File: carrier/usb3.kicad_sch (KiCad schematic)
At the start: 48 parts, among them J13 USB3_A, U16 W25X40CLUXIG, U18 AP2191, U19 uPD720202, U5 TPD4EUSB30, Y1 24MHz

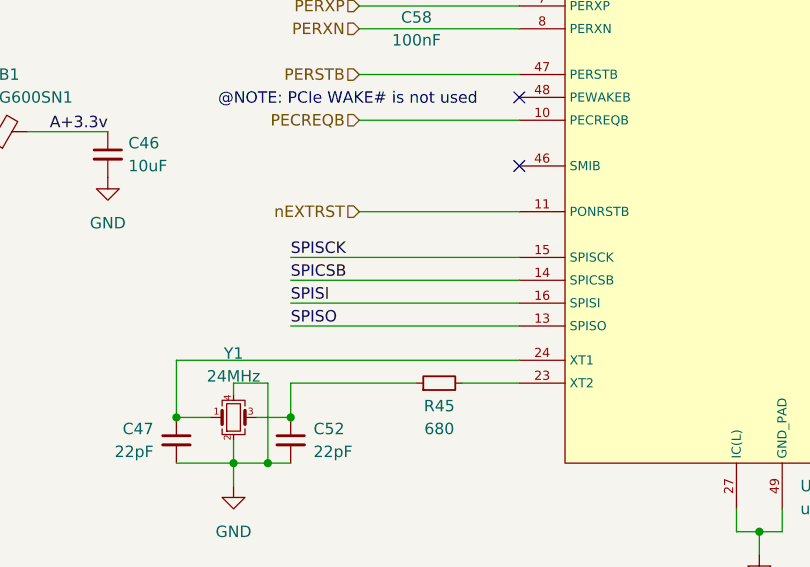
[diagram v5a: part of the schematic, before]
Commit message: Feat[carrier]: v3 ordered
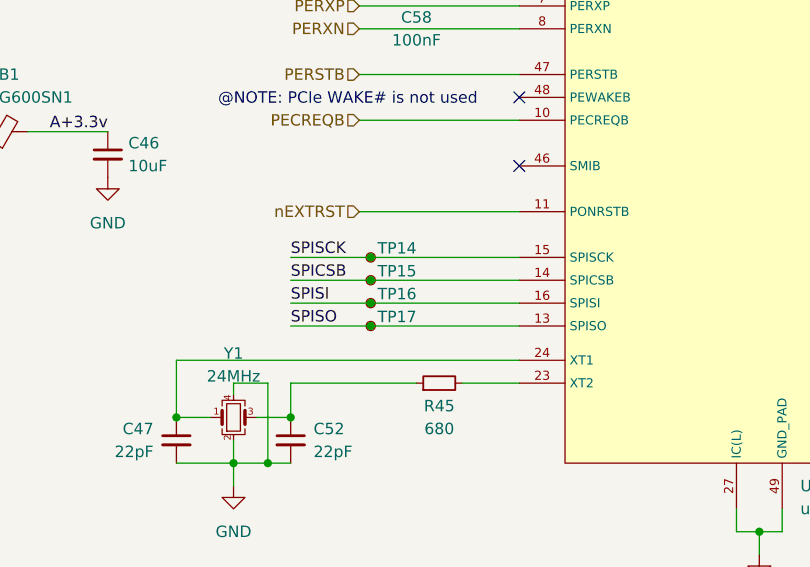
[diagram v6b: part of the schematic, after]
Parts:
- added TP14, TP15, TP16, TP17: ~, TestPoint:TestPoint_Pad_D1.5mm, symbol Connector:TestPoint_Small
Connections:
- net SPICSB: now also TP15.1
- net SPISCK: now also TP14.1
- net SPISI: now also TP16.1
- net SPISO: now also TP17.1
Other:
- company: (none) -> MUREX Robotics [Byran Huang]
- title: (none) -> Carrier Board
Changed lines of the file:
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@@
 (kicad_sch (version 20230819) (generator eeschema)
   (paper "A4")
+  (title_block
+    (title "Carrier Board")
+    (date "2023-12-09")
+    (rev "V3")
+    (company "MUREX Robotics [Byran Huang]")
+    (comment 1 "//DO IT RIGHT,  DO IT MUREX")
+    (comment 2 "// ATTEMPT THE IMPOSSIBLE")
+    (comment 3 "CM4-based ROV (robotics) control board.")
+    (comment 4 "The MUREX Carrier Board is the world's first open-source ")
+  )
   (junction (at 45.72 26.67) (diameter 0) (color 0 0 0 0)
   )
@@
   (junction (at 45.72 41.91) (diameter 0) (color 0 0 0 0)
   )
+  (junction (at 85.09 92.71) (diameter 0) (color 0 0 0 0)
+  )
   (junction (at 204.47 86.36) (diameter 0) (color 0 0 0 0)
   )
@@
   (junction (at 128.27 123.19) (diameter 0) (color 0 0 0 0)
   )
+  (junction (at 85.09 100.33) (diameter 0) (color 0 0 0 0)
+  )
   (junction (at 106.68 31.75) (diameter 0) (color 0 0 0 0)
   )
@@
   (junction (at 63.5 110.49) (diameter 0) (color 0 0 0 0)
   )
+  (junction (at 85.09 97.79) (diameter 0) (color 0 0 0 0)
+  )
   (junction (at 35.56 26.67) (diameter 0) (color 0 0 0 0)
   )
@@
   )
   (junction (at 86.36 26.67) (diameter 0) (color 0 0 0 0)
+  )
+  (junction (at 85.09 95.25) (diameter 0) (color 0 0 0 0)
   )
   (junction (at 156.21 31.75) (diameter 0) (color 0 0 0 0)
@@
     (stroke (width 0) (type default))
   )
+  (wire (pts (xy 85.09 97.79) (xy 101.6 97.79))
+    (stroke (width 0) (type default))
+  )
   (wire (pts (xy 86.36 41.91) (xy 96.52 41.91))
     (stroke (width 0) (type default))
@@
     (stroke (width 0) (type default))
   )
-  (wire (pts (xy 76.2 92.71) (xy 101.6 92.71))
+  (wire (pts (xy 76.2 92.71) (xy 85.09 92.71))
     (stroke (width 0) (type default))
   )
@@
     (stroke (width 0) (type default))
   )
-  (wire (pts (xy 76.2 95.25) (xy 101.6 95.25))
+  (wire (pts (xy 76.2 95.25) (xy 85.09 95.25))
     (stroke (width 0) (type default))
   )
@@
     (stroke (width 0) (type default))
   )
+  (wire (pts (xy 85.09 95.25) (xy 101.6 95.25))
+    (stroke (width 0) (type default))
+  )
   (wire (pts (xy 63.5 115.57) (xy 69.85 115.57))
     (stroke (width 0) (type default))
@@
     (stroke (width 0) (type default))
   )
-  (wire (pts (xy 76.2 97.79) (xy 101.6 97.79))
+  (wire (pts (xy 85.09 92.71) (xy 101.6 92.71))
+    (stroke (width 0) (type default))
+  )
+  (wire (pts (xy 76.2 97.79) (xy 85.09 97.79))
     (stroke (width 0) (type default))
   )
@@
     (stroke (width 0) (type default))
   )
+  (wire (pts (xy 85.09 100.33) (xy 101.6 100.33))
+    (stroke (width 0) (type default))
+  )
   (wire (pts (xy 154.94 76.2) (xy 166.37 76.2))
     (stroke (width 0) (type default))
@@
     (stroke (width 0) (type default))
   )
-  (wire (pts (xy 76.2 100.33) (xy 101.6 100.33))
+  (wire (pts (xy 76.2 100.33) (xy 85.09 100.33))
     (stroke (width 0) (type default))
   )
@@
         (path "/4b1cea9d-93bc-4380-88c3-ede99bb53de2/4da56470-0b67-4551-923f-8b4b216ded57/7428a731-2323-481a-bc64-c9fb631cc98e"
           (reference "R50") (unit 1)
+        )
+      )
+    )
+  )
+  (symbol (lib_id "Connector:TestPoint_Small") (at 85.09 100.33 180) (unit 1)
+    (exclude_from_sim no) (in_bom yes) (on_board yes) (dnp no)
+    (property "Reference" "TP17" (at 85.852 99.314 0)
+      (effects (font (size 1.27 1.27)) (justify right))
+    )
+    (property "Value" "~" (at 83.82 99.0601 0)
+      (effects (font (size 1.27 1.27)) (justify left))
+    )
+    (property "Footprint" "TestPoint:TestPoint_Pad_D1.5mm" (at 80.01 100.33 0)
+      (effects (font (size 1.27 1.27)) hide)
+    )
+    (property "Datasheet" "~" (at 80.01 100.33 0)
+      (effects (font (size 1.27 1.27)) hide)
+    )
+    (property "Description" "test point" (at 85.09 100.33 0)
+      (effects (font (size 1.27 1.27)) hide)
+    )
+    (pin "1")
+    (instances
+      (project "carrier"
+        (path "/4b1cea9d-93bc-4380-88c3-ede99bb53de2/4da56470-0b67-4551-923f-8b4b216ded57/7428a731-2323-481a-bc64-c9fb631cc98e"
+          (reference "TP17") (unit 1)
+        )
+      )
+    )
+  )
+  (symbol (lib_id "Connector:TestPoint_Small") (at 85.09 92.71 180) (unit 1)
+    (exclude_from_sim no) (in_bom yes) (on_board yes) (dnp no)
+    (property "Reference" "TP14" (at 85.852 91.694 0)
+      (effects (font (size 1.27 1.27)) (justify right))
+    )
+    (property "Value" "~" (at 83.82 91.4401 0)
+      (effects (font (size 1.27 1.27)) (justify left))
+    )
+    (property "Footprint" "TestPoint:TestPoint_Pad_D1.5mm" (at 80.01 92.71 0)
+      (effects (font (size 1.27 1.27)) hide)
+    )
+    (property "Datasheet" "~" (at 80.01 92.71 0)
+      (effects (font (size 1.27 1.27)) hide)
+    )
+    (property "Description" "test point" (at 85.09 92.71 0)
+      (effects (font (size 1.27 1.27)) hide)
+    )
+    (pin "1")
+    (instances
+      (project "carrier"
+        (path "/4b1cea9d-93bc-4380-88c3-ede99bb53de2/4da56470-0b67-4551-923f-8b4b216ded57/7428a731-2323-481a-bc64-c9fb631cc98e"
+          (reference "TP14") (unit 1)
         )
       )
@@
     )
   )
+  (symbol (lib_id "Connector:TestPoint_Small") (at 85.09 97.79 180) (unit 1)
+    (exclude_from_sim no) (in_bom yes) (on_board yes) (dnp no)
+    (property "Reference" "TP16" (at 85.852 96.774 0)
+      (effects (font (size 1.27 1.27)) (justify right))
+    )
+    (property "Value" "~" (at 83.82 96.5201 0)
+      (effects (font (size 1.27 1.27)) (justify left))
+    )
+    (property "Footprint" "TestPoint:TestPoint_Pad_D1.5mm" (at 80.01 97.79 0)
+      (effects (font (size 1.27 1.27)) hide)
+    )
+    (property "Datasheet" "~" (at 80.01 97.79 0)
+      (effects (font (size 1.27 1.27)) hide)
+    )
+    (property "Description" "test point" (at 85.09 97.79 0)
+      (effects (font (size 1.27 1.27)) hide)
+    )
+    (pin "1")
+    (instances
+      (project "carrier"
+        (path "/4b1cea9d-93bc-4380-88c3-ede99bb53de2/4da56470-0b67-4551-923f-8b4b216ded57/7428a731-2323-481a-bc64-c9fb631cc98e"
+          (reference "TP16") (unit 1)
+        )
+      )
+    )
+  )
   (symbol (lib_id "power:GND") (at 69.85 118.11 0) (unit 1)
     (exclude_from_sim no) (in_bom yes) (on_board yes) (dnp no) (fields_autoplaced)
@@
         )
       )
+    )
+  )
+  (symbol (lib_id "Connector:TestPoint_Small") (at 85.09 95.25 180) (unit 1)
+    (exclude_from_sim no) (in_bom yes) (on_board yes) (dnp no)
+    (property "Reference" "TP15" (at 85.852 94.234 0)
+      (effects (font (size 1.27 1.27)) (justify right))
+    )
+    (property "Value" "~" (at 83.82 93.9801 0)
+      (effects (font (size 1.27 1.27)) (justify left))
+    )
+    (property "Footprint" "TestPoint:TestPoint_Pad_D1.5mm" (at 80.01 95.25 0)
+      (effects (font (size 1.27 1.27)) hide)
+    )
+    (property "Datasheet" "~" (at 80.01 95.25 0)
+      (effects (font (size 1.27 1.27)) hide)
+    )
+    (property "Description" "test point" (at 85.09 95.25 0)
+      (effects (font (size 1.27 1.27)) hide)
+    )
+    (pin "1")
+    (instances
+      (project "carrier"
+        (path "/4b1cea9d-93bc-4380-88c3-ede99bb53de2/4da56470-0b67-4551-923f-8b4b216ded57/7428a731-2323-481a-bc64-c9fb631cc98e"
+          (reference "TP15") (unit 1)
+        )
+      )

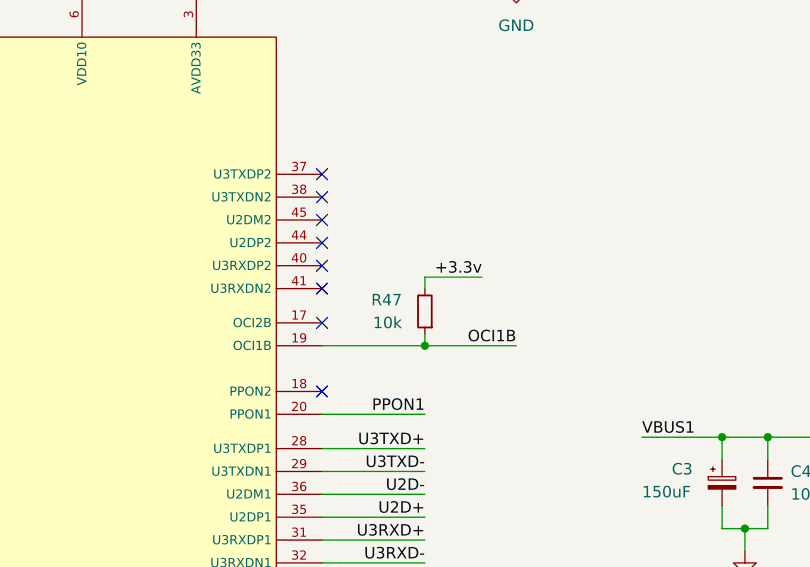
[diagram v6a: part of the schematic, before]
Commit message: Fix: updated carrier board to v3.1
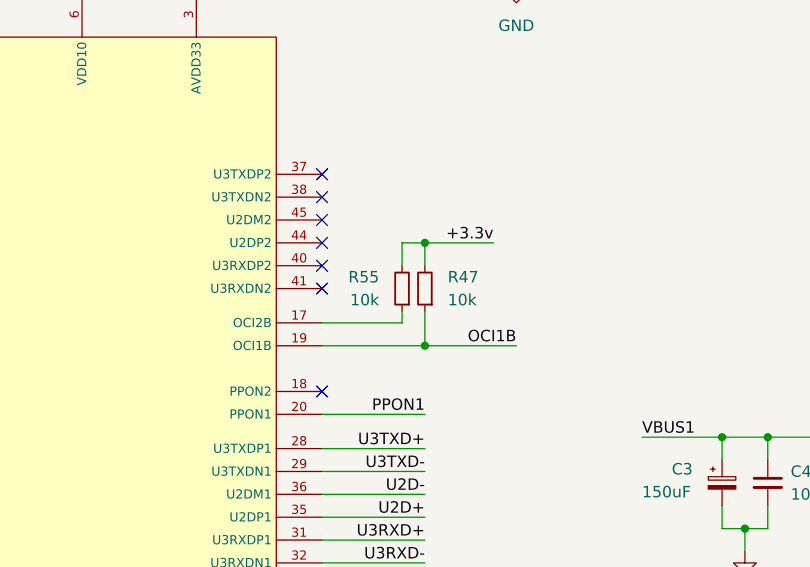
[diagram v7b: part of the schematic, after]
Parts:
- added R55: 10k, Resistor_SMD:R_0402_1005Metric, symbol Device:R_Small
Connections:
- net +3.3v: now also R55.2
- net at U19.17 (OCI2B): now also R55.1
- no-connect marks 12 -> 11
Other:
- moved on the sheet: R47
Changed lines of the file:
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@@
   (title_block
     (title "Carrier Board")
-    (date "2023-12-09")
-    (rev "V3")
+    (date "2023-12-30")
+    (rev "V3.1")
     (company "MUREX Robotics [Byran Huang]")
     (comment 1 "//DO IT RIGHT,  DO IT MUREX")
@@
   (junction (at 96.52 26.67) (diameter 0) (color 0 0 0 0)
   )
+  (junction (at 166.37 64.77) (diameter 0) (color 0 0 0 0)
+  )
   (junction (at 201.93 96.52) (diameter 0) (color 0 0 0 0)
   )
@@
   (no_connect (at 154.94 57.15))
   (no_connect (at 154.94 64.77))
-  (no_connect (at 154.94 73.66))
   (no_connect (at 101.6 82.55))
   (no_connect (at 101.6 74.93))
@@
     (stroke (width 0) (type default))
   )
-  (wire (pts (xy 166.37 74.93) (xy 166.37 76.2))
+  (wire (pts (xy 166.37 72.39) (xy 166.37 76.2))
     (stroke (width 0) (type default))
   )
@@
     (stroke (width 0) (type default))
   )
+  (wire (pts (xy 154.94 73.66) (xy 163.83 73.66))
+    (stroke (width 0) (type default))
+  )
   (wire (pts (xy 72.39 110.49) (xy 76.2 110.49))
     (stroke (width 0) (type default))
@@
     (stroke (width 0) (type default))
   )
-  (wire (pts (xy 166.37 68.58) (xy 172.72 68.58))
+  (wire (pts (xy 166.37 64.77) (xy 173.99 64.77))
     (stroke (width 0) (type default))
   )
@@
     (stroke (width 0) (type default))
   )
+  (wire (pts (xy 163.83 72.39) (xy 163.83 73.66))
+    (stroke (width 0) (type default))
+  )
   (wire (pts (xy 190.5 86.36) (xy 199.39 86.36))
     (stroke (width 0) (type default))
@@
     (stroke (width 0) (type default))
   )
+  (wire (pts (xy 163.83 67.31) (xy 163.83 64.77))
+    (stroke (width 0) (type default))
+  )
   (wire (pts (xy 176.53 31.75) (xy 176.53 35.56))
     (stroke (width 0) (type default))
@@
     (stroke (width 0) (type default))
   )
-  (wire (pts (xy 166.37 68.58) (xy 166.37 69.85))
+  (wire (pts (xy 166.37 64.77) (xy 166.37 67.31))
+    (stroke (width 0) (type default))
+  )
+  (wire (pts (xy 163.83 64.77) (xy 166.37 64.77))
     (stroke (width 0) (type default))
   )
@@
     (effects (font (size 1.27 1.27)) (justify left bottom))
   )
-  (label "+3.3v" (at 172.72 68.58 180) (fields_autoplaced)
+  (label "+3.3v" (at 173.99 64.77 180) (fields_autoplaced)
     (effects (font (size 1.27 1.27)) (justify right bottom))
   )
@@
     )
   )
-  (symbol (lib_id "Device:R_Small") (at 166.37 72.39 180) (unit 1)
-    (exclude_from_sim no) (in_bom yes) (on_board yes) (dnp no) (fields_autoplaced)
-    (property "Reference" "R47" (at 163.83 71.1199 0)
-      (effects (font (size 1.27 1.27)) (justify left))
-    )
-    (property "Value" "10k" (at 163.83 73.6599 0)
-      (effects (font (size 1.27 1.27)) (justify left))
-    )
-    (property "Footprint" "Resistor_SMD:R_0402_1005Metric" (at 166.37 72.39 0)
-      (effects (font (size 1.27 1.27)) hide)
-    )
-    (property "Datasheet" "~" (at 166.37 72.39 0)
-      (effects (font (size 1.27 1.27)) hide)
-    )
-    (property "Description" "Resistor, small symbol" (at 166.37 72.39 0)
+  (symbol (lib_id "Device:R_Small") (at 166.37 69.85 180) (unit 1)
+    (exclude_from_sim no) (in_bom yes) (on_board yes) (dnp no) (fields_autoplaced)
+    (property "Reference" "R47" (at 168.91 68.5799 0)
+      (effects (font (size 1.27 1.27)) (justify right))
+    )
+    (property "Value" "10k" (at 168.91 71.1199 0)
+      (effects (font (size 1.27 1.27)) (justify right))
+    )
+    (property "Footprint" "Resistor_SMD:R_0402_1005Metric" (at 166.37 69.85 0)
+      (effects (font (size 1.27 1.27)) hide)
+    )
+    (property "Datasheet" "~" (at 166.37 69.85 0)
+      (effects (font (size 1.27 1.27)) hide)
+    )
+    (property "Description" "Resistor, small symbol" (at 166.37 69.85 0)
       (effects (font (size 1.27 1.27)) hide)
     )
@@
         )
       )
+    )
+  )
+  (symbol (lib_id "Device:R_Small") (at 163.83 69.85 180) (unit 1)
+    (exclude_from_sim no) (in_bom yes) (on_board yes) (dnp no) (fields_autoplaced)
+    (property "Reference" "R55" (at 161.29 68.5799 0)
+      (effects (font (size 1.27 1.27)) (justify left))
+    )
+    (property "Value" "10k" (at 161.29 71.1199 0)
+      (effects (font (size 1.27 1.27)) (justify left))
+    )
+    (property "Footprint" "Resistor_SMD:R_0402_1005Metric" (at 163.83 69.85 0)
+      (effects (font (size 1.27 1.27)) hide)
+    )
+    (property "Datasheet" "~" (at 163.83 69.85 0)
+      (effects (font (size 1.27 1.27)) hide)
+    )
+    (property "Description" "Resistor, small symbol" (at 163.83 69.85 0)
+      (effects (font (size 1.27 1.27)) hide)
+    )
+    (pin "1")
+    (pin "2")
+    (instances
+      (project "carrier"
+        (path "/4b1cea9d-93bc-4380-88c3-ede99bb53de2/4da56470-0b67-4551-923f-8b4b216ded57/7428a731-2323-481a-bc64-c9fb631cc98e"
+          (reference "R55") (unit 1)
+        )
+      )

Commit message: Feat: float sid
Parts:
- renumbered C3 to C66, C4 to C68, C9 to C74, R8 to R50, TP1 to TP10, TP1 to TP11, U5 to U17, U5 to U20
